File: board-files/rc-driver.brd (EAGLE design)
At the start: 27 x 14 mm, 13 parts, among them IC1 TINY22S

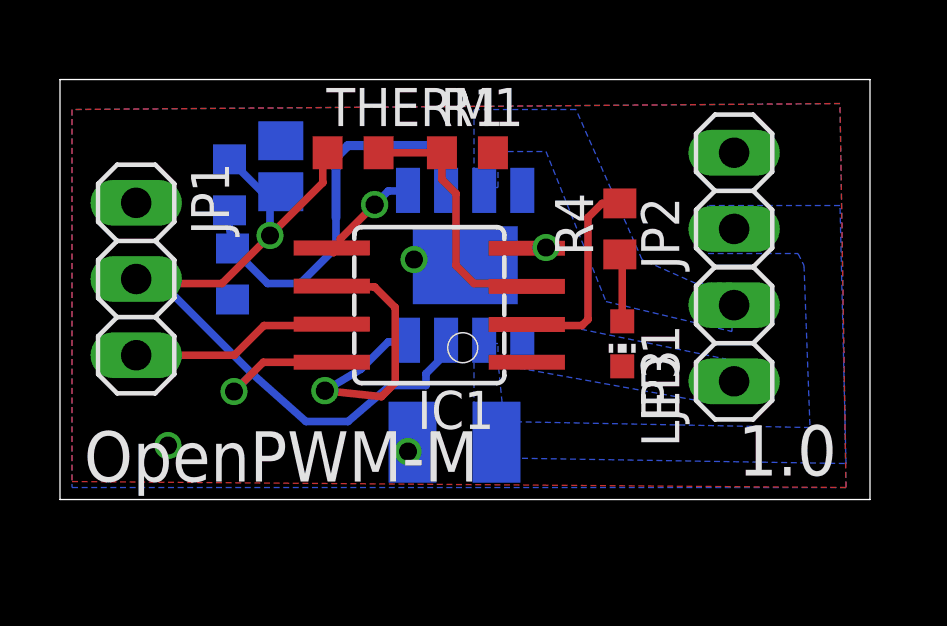
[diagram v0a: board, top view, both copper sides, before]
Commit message: Added start os v 2.0 files. Need to connect vref.
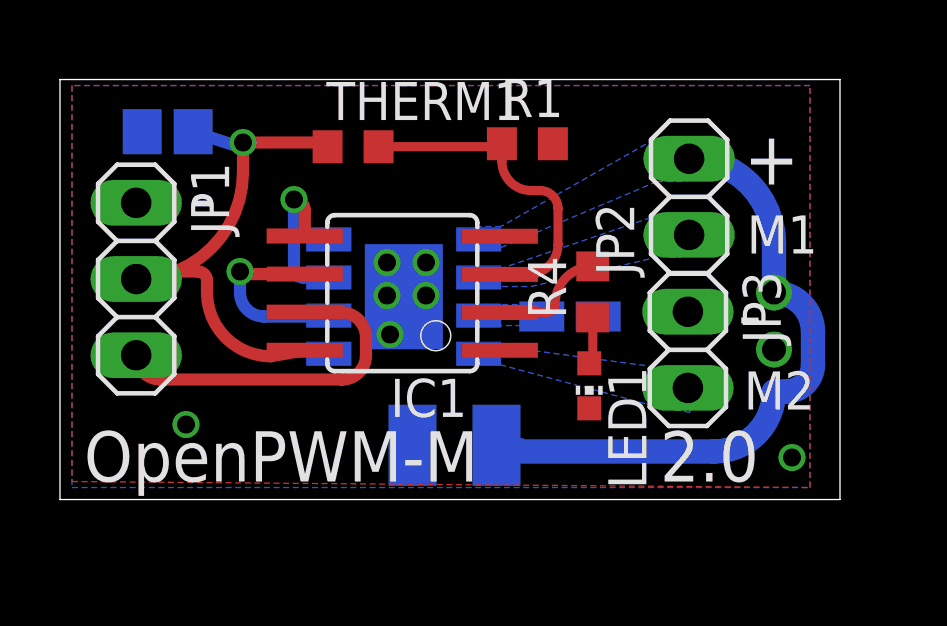
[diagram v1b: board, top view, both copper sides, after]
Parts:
- removed R3: (no value), resistor:R0603
- R2: device resistor:R0603 -> resistor:R0805W
- U$1: value ZXBM5210-MOTOR-DRIVER -> A4950-HBRIDGE
- moved R2 12.2 mm to (17.0, 6.10), turned to 0 degrees
- moved C3 3.94 mm to (3.59, 12.3), turned to 180 degrees
- moved R4 2.28 mm to (17.8, 6.92)
- moved U$1 2.10 mm to (11.5, 6.90), turned to 90 degrees
- moved R1 2.02 mm to (15.6, 11.9)
- moved LED1 1.78 mm to (17.6, 3.79)
- moved JP3 1.56 mm to (20.9, 4.99), turned to 270 degrees
- moved JP2 1.51 mm to (21.0, 10.1)
- moved IC1 0.98 mm to (11.4, 6.88)
- moved THERM1 0.20 mm to (9.77, 11.8)
- moved C1 0.10 mm to (13.2, 1.81)
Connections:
- removed net N$1: R2.2, R3.1, U$1.P$6
- new net LSS: R2.2, U$1.P$7
- new net N$11: U$1.P$4
- net FWD: now also IC1.5, U$1.P$3; no longer IC1.6, U$1.P$4
- net GND: now also JP3.1, R2.1, U$1.P$1; no longer JP2.2, R3.2, U$1.P$8
- net MOTOR1-1: now also JP2.1, U$1.P$6; no longer JP3.1, U$1.P$1
- net MOTOR1-2: now also U$1.P$8; no longer U$1.P$7
- net REV: now also IC1.6, U$1.P$2; no longer IC1.5, U$1.P$5
- net VCC: no longer R2.1, U$1.P$3
- net VM: now also JP2.2, U$1.P$5; no longer JP2.1, U$1.P$2
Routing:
- net VM: track 0.00 -> 20.6 mm, vias 0 -> 1
- net N$1: track 14.1 -> 0.00 mm
- net VCC: track 30.8 -> 17.8 mm, vias 2 -> 1
- net FWD: track 10.8 -> 4.95 mm
- net PWM-1: track 6.95 -> 11.3 mm
- net N$2: track 6.79 -> 3.74 mm
- net REV: track 3.64 -> 6.20 mm
- net TEMP: track 8.71 -> 10.8 mm
- net N$3: track 2.26 -> 1.58 mm
- added copper zone on layer 16, net LSS
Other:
- board size 27 x 14 mm -> 26 x 14 mm
- board text added: "+"
- board text added: "-"
- board text added: "2.0"
- board text added: "C1"
- board text added: "M1"
- board text added: "M2"
- board text removed: "1.0"

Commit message: Adding RC net to VREF. Creating gerbers for plain board.
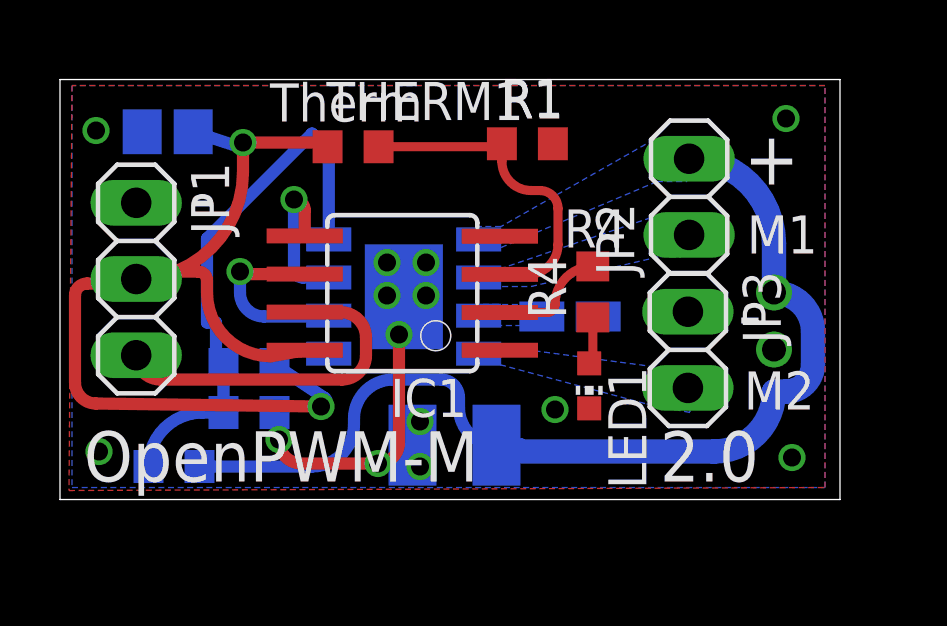
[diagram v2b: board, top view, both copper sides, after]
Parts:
- added R3, R5, R6: (no value), resistor:R0603
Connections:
- removed net N$11: U$1.P$4
- new net N$1: R3.2, R5.1, R6.2, U$1.P$4
- net GND: now also R5.2
- net VCC: now also R3.1
- net VM: now also R6.1
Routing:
- net N$1: track 0.00 -> 18.1 mm
- net VCC: track 17.8 -> 33.8 mm, vias 1 -> 2
- net VM: track 20.6 -> 33.0 mm
- net GND: track 0.00 -> 10.7 mm, vias 8 -> 15
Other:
- board text added: "C3"
- board text added: "R1"
- board text added: "R2"
- board text added: "R3"
- board text added: "R4"
- board text added: "R5"
- board text added: "R6"
- board text added: "Therm"
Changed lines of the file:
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@@
 <layer number="19" name="Unrouted" color="6" fill="1" visible="yes" active="yes"/>
 <layer number="20" name="Dimension" color="15" fill="1" visible="yes" active="yes"/>
-<layer number="21" name="tPlace" color="7" fill="1" visible="yes" active="yes"/>
+<layer number="21" name="tPlace" color="7" fill="1" visible="no" active="yes"/>
 <layer number="22" name="bPlace" color="7" fill="1" visible="yes" active="yes"/>
 <layer number="23" name="tOrigins" color="15" fill="1" visible="yes" active="yes"/>
@@
 <text x="5.2" y="9.2" size="1.778" layer="22" rot="MR0">-</text>
 <text x="4.4" y="9.2" size="1.778" layer="21">-</text>
+<text x="17.7" y="7.2" size="1.27" layer="22" ratio="15" rot="MR0">R2</text>
+<text x="6.4" y="9.9" size="1.27" layer="22" ratio="15" rot="MR0">C3</text>
+<text x="7.9" y="1" size="1.27" layer="22" ratio="15" rot="MR0">R5</text>
+<text x="7.2" y="5.4" size="1.27" layer="22" ratio="15" rot="MR0">R3</text>
+<text x="7" y="12.6" size="1.27" layer="21" ratio="15">Therm</text>
+<text x="14.7" y="12.7" size="1.27" layer="21" ratio="15">R1</text>
+<text x="16.8" y="8.4" size="1.27" layer="21" ratio="15">R4</text>
+<text x="4" y="1.7" size="1.016" layer="22" ratio="14" rot="MR0">R6</text>
 </plain>
 <attributes>
@@
 <element name="U$1" library="mgregg" package="SO-8EP" value="A4950-HBRIDGE" x="11.5" y="6.9" rot="MR90"/>
 <element name="R2" library="resistor" package="R0805W" value="" x="17" y="6.1" rot="MR0"/>
+<element name="R3" library="resistor" package="R0603" value="" x="6.3" y="4.5" rot="MR0"/>
+<element name="R5" library="resistor" package="R0603" value="" x="6.3" y="2.9" rot="MR180"/>
+<element name="R6" library="resistor" package="R0603" value="" x="3.8" y="1.1" rot="MR0"/>
 </elements>
 <signals>
@@
 <contactref element="LED1" pad="C"/>
 <polygon width="0.254" layer="1" thermals="no" rank="6">
-<vertex x="25" y="13.8"/>
+<vertex x="25.5" y="13.8"/>
 <vertex x="0.4" y="13.8"/>
-<vertex x="0.4" y="0.6"/>
-<vertex x="25" y="0.4"/>
+<vertex x="0.3" y="0.3"/>
+<vertex x="25.5" y="0.4"/>
 </polygon>
 <polygon width="0.254" layer="16" isolate="0.254" thermals="no" rank="6">
-<vertex x="25" y="0.4"/>
-<vertex x="25" y="13.8"/>
+<vertex x="25.5" y="0.4"/>
+<vertex x="25.5" y="13.8"/>
 <vertex x="0.4" y="13.8"/>
 <vertex x="0.4" y="0.4"/>
 </polygon>
-<via x="4.2" y="2.5" extent="1-16" drill="0.6"/>
+<via x="1.3" y="1.6" extent="1-16" drill="0.6"/>
 <via x="24.4" y="1.4" extent="1-16" drill="0.6"/>
 <contactref element="U$1" pad="P$1"/>
@@
 <contactref element="R2" pad="1"/>
 <via x="12.2" y="6.8" extent="1-16" drill="0.6"/>
-<via x="11" y="5.5" extent="1-16" drill="0.6"/>
+<via x="11.3" y="5.5" extent="1-16" drill="0.6"/>
 <via x="12.2" y="7.9" extent="1-16" drill="0.6"/>
 <via x="10.9" y="6.8" extent="1-16" drill="0.6"/>
@@
 <via x="23.8" y="5" extent="1-16" drill="0.8"/>
 <contactref element="JP3" pad="1"/>
+<contactref element="R5" pad="2"/>
+<wire x1="11.75" y1="1.81" x2="11.14" y2="1.2" width="0.4064" layer="16" curve="-90"/>
+<wire x1="11.14" y1="1.2" x2="10.6" y2="1.2" width="0.4064" layer="16"/>
+<via x="10.6" y="1.2" extent="1-16" drill="0.6" shape="square"/>
+<wire x1="10.6" y1="1.2" x2="11.3" y2="1.9" width="0.4064" layer="1" curve="90"/>
+<wire x1="11.3" y1="1.9" x2="11.3" y2="5.5" width="0.4064" layer="1"/>
+<wire x1="7.15" y1="2.9" x2="7.3" y2="2.85" width="0.4064" layer="16" curve="-90"/>
+<wire x1="7.3" y1="2.85" x2="7.3" y2="2" width="0.4064" layer="16"/>
+<via x="7.3" y="2" extent="1-16" drill="0.6" shape="square"/>
+<wire x1="7.3" y1="2" x2="8" y2="1.2" width="0.4064" layer="1" curve="90"/>
+<wire x1="8" y1="1.2" x2="10.6" y2="1.2" width="0.4064" layer="1"/>
+<via x="12" y="2.6" extent="1-16" drill="0.6"/>
+<via x="12" y="1.1" extent="1-16" drill="0.6"/>
+<via x="16.5" y="3" extent="1-16" drill="0.6"/>
+<via x="1.2" y="12.3" extent="1-16" drill="0.6"/>
+<via x="24.2" y="12.7" extent="1-16" drill="0.6"/>
 </signal>
 <signal name="VM">
@@
 <wire x1="25.1" y1="4.5" x2="25.1" y2="5.6" width="0.8128" layer="16"/>
 <wire x1="25.1" y1="5.6" x2="23.8" y2="6.9" width="0.8128" layer="16" curve="90"/>
+<contactref element="R6" pad="1"/>
+<wire x1="4.65" y1="1.1" x2="8.4" y2="1.1" width="0.4064" layer="16"/>
+<wire x1="8.4" y1="1.1" x2="9.8" y2="2.5" width="0.4064" layer="16" curve="90"/>
+<wire x1="9.8" y1="2.5" x2="9.8" y2="2.7" width="0.4064" layer="16"/>
+<wire x1="9.8" y1="2.7" x2="11.1" y2="4" width="0.4064" layer="16" curve="-90"/>
+<wire x1="11.1" y1="4" x2="12.7" y2="4" width="0.4064" layer="16"/>
+<wire x1="12.7" y1="4" x2="13.3" y2="3.4" width="0.4064" layer="16" curve="-90"/>
+<wire x1="13.3" y1="3.4" x2="13.3" y2="3.06" width="0.4064" layer="16"/>
+<wire x1="13.3" y1="3.06" x2="14.55" y2="1.81" width="0.4064" layer="16" curve="90"/>
 </signal>
 <signal name="VCC">
@@
 <wire x1="4.6" y1="7.6" x2="2.79" y2="7.6" width="0.4064" layer="1"/>
 <wire x1="2.79" y1="7.6" x2="2.54" y2="7.35" width="0.4064" layer="1" curve="90"/>
+<contactref element="R3" pad="1"/>
+<wire x1="7.15" y1="4.5" x2="8.8" y2="3.4" width="0.4064" layer="16"/>
+<wire x1="8.8" y1="3.4" x2="8.7" y2="3.1" width="0.4064" layer="16" curve="-165.749967"/>
+<via x="8.7" y="3.1" extent="1-16" drill="0.6"/>
+<wire x1="8.7" y1="3.1" x2="1.2" y2="3.2" width="0.4064" layer="1"/>
+<wire x1="1.2" y1="3.2" x2="0.5" y2="3.9" width="0.4064" layer="1" curve="-90"/>
+<wire x1="0.5" y1="3.9" x2="0.5" y2="6.8" width="0.4064" layer="1"/>
+<wire x1="0.5" y1="6.8" x2="0.9" y2="7.2" width="0.4064" layer="1" curve="-90"/>
+<wire x1="0.9" y1="7.2" x2="2.39" y2="7.2" width="0.4064" layer="1"/>
+<wire x1="2.39" y1="7.2" x2="2.54" y2="7.35" width="0.4064" layer="1" curve="90"/>
 </signal>
 <signal name="PWM-1">
@@
 <wire x1="17.76" y1="4.66" x2="17.64" y2="4.54" width="0.3048" layer="1" curve="-90"/>
 </signal>
-<signal name="N$11">
-<contactref element="U$1" pad="P$4"/>
-</signal>
 <signal name="LSS">
 <contactref element="U$1" pad="P$7"/>
@@
 </polygon>
 </signal>
+<signal name="N$1">
+<contactref element="R3" pad="2"/>
+<contactref element="R5" pad="1"/>
+<contactref element="U$1" pad="P$4"/>
+<wire x1="5.45" y1="2.9" x2="5.45" y2="4.5" width="0.4064" layer="16"/>
+<wire x1="5.45" y1="4.5" x2="5.2" y2="4.8" width="0.4064" layer="16"/>
+<wire x1="5.2" y1="4.8" x2="5.2" y2="5.9" width="0.4064" layer="16"/>
+<wire x1="5.2" y1="5.9" x2="4.9" y2="5.9" width="0.4064" layer="16"/>
+<wire x1="4.9" y1="5.9" x2="4.9" y2="8.7" width="0.4064" layer="16"/>
+<wire x1="4.9" y1="8.7" x2="8.4" y2="12.2" width="0.4064" layer="16"/>
+<wire x1="8.4" y1="12.2" x2="8.96" y2="11.64" width="0.4064" layer="16"/>
+<wire x1="8.96" y1="11.64" x2="8.96" y2="8.67" width="0.4064" layer="16"/>
+<contactref element="R6" pad="2"/>
+<wire x1="2.95" y1="1.1" x2="4.75" y2="2.9" width="0.4064" layer="16" curve="-90"/>
+<wire x1="4.75" y1="2.9" x2="5.45" y2="2.9" width="0.4064" layer="16"/>
+</signal>
 </signals>

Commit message: fixing attiny silk. Shortened single rc-driver board.
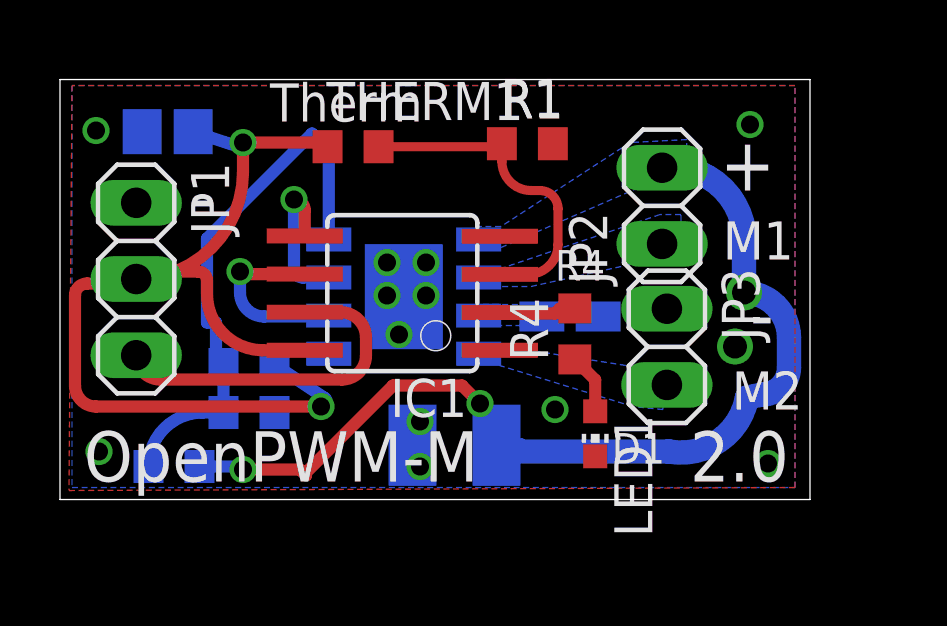
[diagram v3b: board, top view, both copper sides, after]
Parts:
- moved LED1 1.61 mm to (17.8, 2.19)
- moved R4 1.52 mm to (17.2, 5.52)
- moved JP2 0.95 mm to (20.1, 9.79)
- moved JP3 0.71 mm to (20.2, 5.09)
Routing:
- net GND: track 10.7 -> 0.00 mm, vias 15 -> 13
- net N$2: track 3.74 -> 2.58 mm
- net VM: track 33.0 -> 32.6 mm, vias 1 -> 3
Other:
- board size 26 x 14 mm -> 25 x 14 mm
- board text added: "D1"

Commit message: Adding some final touches to the boards. Converting fonts to Vector.
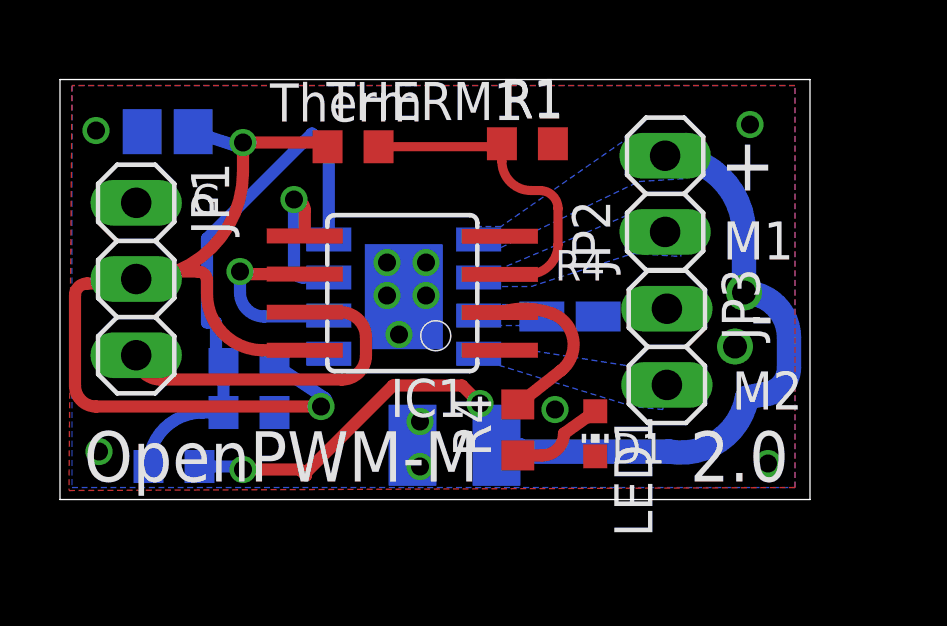
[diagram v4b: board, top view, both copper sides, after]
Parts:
- moved R4 3.72 mm to (15.3, 2.32)
- moved JP2 0.41 mm to (20.2, 10.2)
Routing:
- net N$2: track 2.58 -> 5.54 mm
- net N$3: track 2.01 -> 3.12 mm
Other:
- board text added: "G"
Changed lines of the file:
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@@
 <?xml version="1.0" encoding="utf-8"?>
 <!DOCTYPE eagle SYSTEM "eagle.dtd">
-<eagle version="7.1.0">
+<eagle version="7.2.0">
 <drawing>
 <settings>
-<setting alwaysvectorfont="no"/>
+<setting alwaysvectorfont="yes"/>
 <setting verticaltext="up"/>
 </settings>
 <grid distance="0.1" unitdist="mm" unit="mm" style="lines" multiple="1" display="no" altdistance="0.1" altunitdist="mm" altunit="mm"/>
 <layers>
-<layer number="1" name="Top" color="4" fill="1" visible="no" active="yes"/>
+<layer number="1" name="Top" color="4" fill="1" visible="yes" active="yes"/>
 <layer number="16" name="Bottom" color="1" fill="1" visible="yes" active="yes"/>
 <layer number="17" name="Pads" color="2" fill="1" visible="yes" active="yes"/>
@@
 <layer number="27" name="tValues" color="7" fill="1" visible="no" active="yes"/>
 <layer number="28" name="bValues" color="7" fill="1" visible="no" active="yes"/>
-<layer number="29" name="tStop" color="7" fill="3" visible="no" active="yes"/>
-<layer number="30" name="bStop" color="7" fill="6" visible="yes" active="yes"/>
-<layer number="31" name="tCream" color="7" fill="4" visible="no" active="yes"/>
+<layer number="29" name="tStop" color="7" fill="3" visible="yes" active="yes"/>
+<layer number="30" name="bStop" color="7" fill="6" visible="no" active="yes"/>
+<layer number="31" name="tCream" color="7" fill="4" visible="yes" active="yes"/>
 <layer number="32" name="bCream" color="7" fill="5" visible="no" active="yes"/>
 <layer number="33" name="tFinish" color="6" fill="3" visible="no" active="yes"/>
@@
 <text x="23.3" y="10.2" size="1.778" layer="22" rot="MR0">+</text>
 <text x="5.2" y="9.2" size="1.778" layer="22" rot="MR0">-</text>
-<text x="4.4" y="9.2" size="1.778" layer="21">-</text>
 <text x="17.7" y="7.2" size="1.27" layer="22" ratio="15" rot="MR0">R2</text>
 <text x="6.4" y="9.9" size="1.27" layer="22" ratio="15" rot="MR0">C3</text>
@@
 <text x="4" y="1.7" size="1.016" layer="22" ratio="14" rot="MR0">R6</text>
 <text x="18.4" y="1.2" size="1.016" layer="21" ratio="15">D1</text>
+<rectangle x1="10.5" y1="6.3" x2="12.5" y2="8.3" layer="29"/>
+<rectangle x1="10.7" y1="5" x2="11.9" y2="6.3" layer="29"/>
+<text x="4.4" y="9.5" size="1.016" layer="21" font="vector" ratio="15">G</text>
 </plain>
 <attributes>
@@
 <element name="THERM1" library="resistor" package="R0603" value="4.7k" x="9.77" y="11.76"/>
 <element name="R1" library="resistor" package="R0603" value="20k" x="15.58" y="11.86"/>
-<element name="R4" library="resistor" package="R0603" value="" x="17.16" y="5.52" rot="R90"/>
+<element name="R4" library="resistor" package="R0603" value="" x="15.26" y="2.32" rot="R90"/>
 <element name="LED1" library="led" package="CHIP-LED0603" value="" x="17.84" y="2.19" rot="R180"/>
-<element name="JP2" library="pinhead" package="1X02" value="" x="20.07" y="9.79" rot="R90"/>
+<element name="JP2" library="pinhead" package="1X02" value="" x="20.17" y="10.19" rot="R90"/>
 <element name="U$1" library="mgregg" package="SO-8EP" value="A4950-HBRIDGE" x="11.5" y="6.9" rot="MR90"/>
 <element name="R2" library="resistor" package="R0805W" value="" x="17" y="6.1" rot="MR0"/>
@@
 <wire x1="20.3" y1="1.6" x2="22.9" y2="3.4" width="0.8128" layer="16" curve="90"/>
 <wire x1="22.8" y1="6.9" x2="22.8" y2="8.93" width="0.8128" layer="16"/>
-<wire x1="22.8" y1="8.93" x2="20.07" y2="11.06" width="0.8128" layer="16" curve="90"/>
+<wire x1="22.8" y1="8.93" x2="20.17" y2="11.46" width="0.8128" layer="16" curve="90"/>
 <polygon width="0.254" layer="16" thermals="no">
 <vertex x="13.9" y="8.4"/>
 <vertex x="14.7" y="8.4"/>
-<vertex x="19.3" y="10.4"/>
-<vertex x="20.8" y="10.4"/>
-<vertex x="20.9" y="12"/>
-<vertex x="19" y="11.9"/>
+<vertex x="19.3" y="10.6"/>
+<vertex x="20.9" y="10.7"/>
+<vertex x="20.9" y="12.2"/>
+<vertex x="19" y="12.1"/>
 <vertex x="14.7" y="9.1"/>
 <vertex x="13.9" y="9.1"/>
@@
 <contactref element="JP2" pad="1"/>
 <polygon width="0.254" layer="16" thermals="no">
-<vertex x="20" y="9.5"/>
+<vertex x="19.2" y="9.6"/>
 <vertex x="14.7" y="7.7"/>
 <vertex x="14.1" y="7.7"/>
 <vertex x="14.1" y="7.1"/>
 <vertex x="15.7" y="7.1"/>
-<vertex x="19.3" y="7.9"/>
-<vertex x="20.7" y="8"/>
-<vertex x="20.7" y="9.5"/>
+<vertex x="19.1" y="8.2"/>
+<vertex x="20.7" y="8.1"/>
+<vertex x="20.6" y="9.6"/>
 </polygon>
 </signal>
@@
 <contactref element="R4" pad="2"/>
 <wire x1="14.6612" y1="6.235" x2="14.6962" y2="6.2" width="0.4064" layer="1"/>
-<wire x1="14.6962" y1="6.2" x2="16.5" y2="6.2" width="0.4064" layer="1"/>
-<wire x1="16.5" y1="6.2" x2="16.67" y2="6.37" width="0.4064" layer="1"/>
-<wire x1="16.67" y1="6.37" x2="17.16" y2="6.37" width="0.4064" layer="1"/>
+<wire x1="15.26" y1="3.17" x2="16.7" y2="4.3" width="0.4064" layer="1"/>
+<wire x1="16.7" y1="4.3" x2="16.4" y2="6.2" width="0.4064" layer="1" curve="121.701102"/>
+<wire x1="16.4" y1="6.2" x2="14.6612" y2="6.235" width="0.4064" layer="1" curve="38.047413"/>
 </signal>
 <signal name="N$3">
 <contactref element="R4" pad="1"/>
 <contactref element="LED1" pad="A"/>
-<wire x1="17.16" y1="4.67" x2="17.84" y2="3.99" width="0.4064" layer="1"/>
-<wire x1="17.84" y1="3.99" x2="17.84" y2="2.94" width="0.4064" layer="1"/>
+<wire x1="15.26" y1="1.47" x2="16.07" y2="1.47" width="0.4064" layer="1"/>
+<wire x1="16.07" y1="1.47" x2="16.8" y2="2.2" width="0.4064" layer="1" curve="90"/>
+<wire x1="16.8" y1="2.2" x2="17.84" y2="2.94" width="0.4064" layer="1"/>
 </signal>
 <signal name="LSS">
